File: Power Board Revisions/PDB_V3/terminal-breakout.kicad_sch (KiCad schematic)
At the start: 13 parts, among them J1 1017507, SW1 SW_SPST, SW13 SW_SPST, SW17 SW_SPST, SW21 SW_SPST, SW5 SW_SPST, SW9 SW_SPST

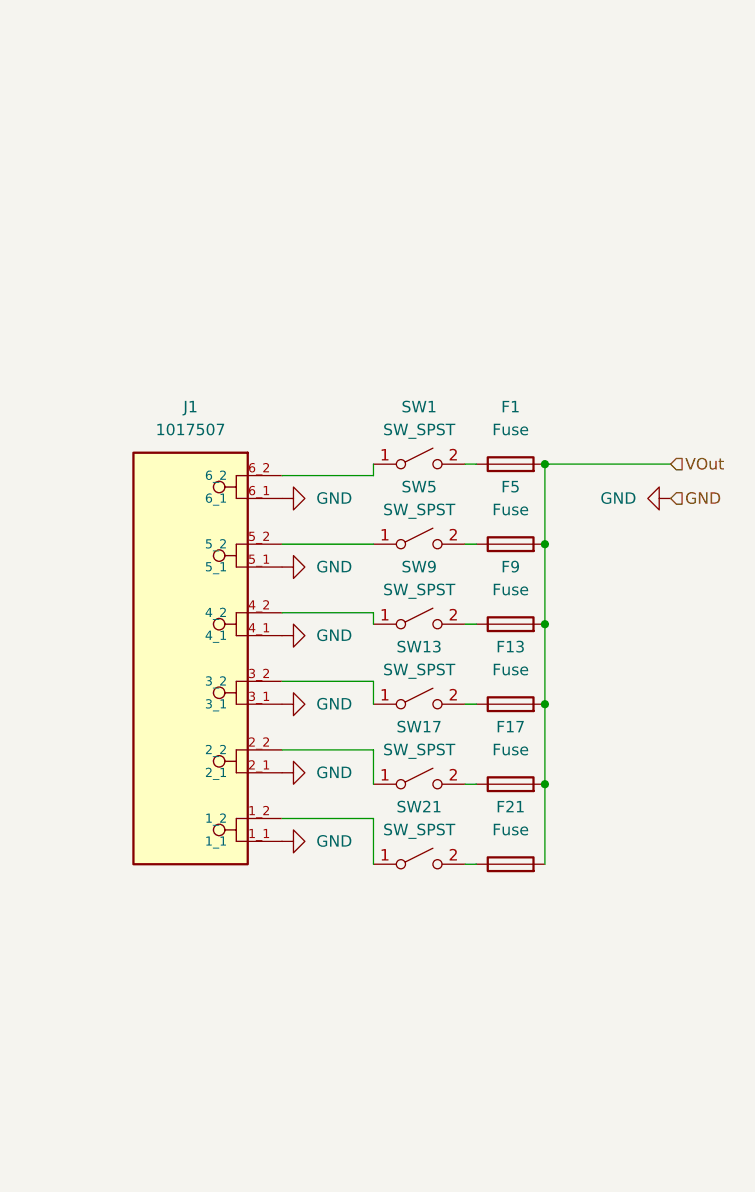
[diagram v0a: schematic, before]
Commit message: Updated PDB V3
I dislike KiCad on windows
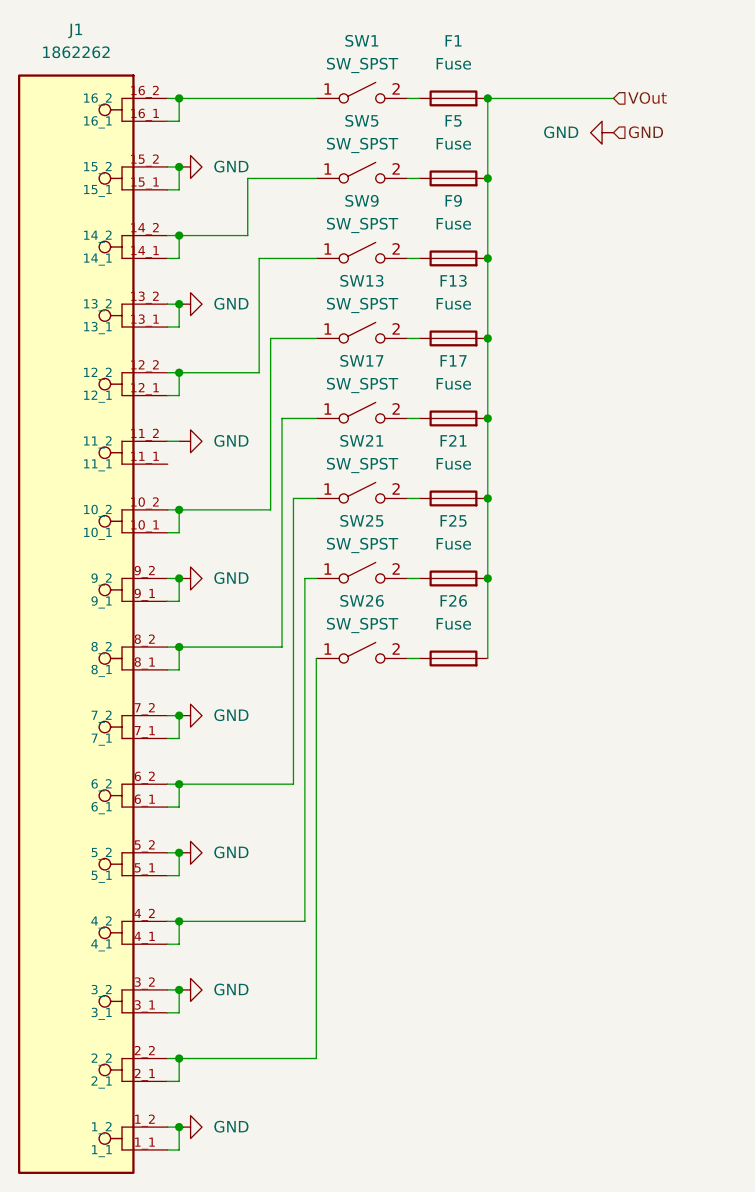
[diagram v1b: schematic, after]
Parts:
- removed J1: 1017507, Footprints:Phoenix 1017507, symbol Symbols:1017507
- added F25, F26: Fuse, Footprints:FUSE_3557-2, symbol Device:Fuse
- added J1: 1862262, Footprints:PHOENIX 1862262, symbol Symbols:1862262
- added SW25, SW26: SW_SPST, Footprints:ESwitch 1101A4CQEA, symbol Switch:SW_SPST
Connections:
- net GND: now also J1.11_2, J1.13_1, J1.13_2, J1.15_1, J1.15_2, J1.1_1, J1.1_2, J1.3_1, J1.3_2, J1.5_1, J1.5_2, J1.7_1, J1.7_2, J1.9_1, J1.9_2
- net VOut: now also F25.2, F26.2
- net at SW9.1 (A): now also J1.12_1, J1.12_2
- net at SW17.1 (A): now also J1.8_1, J1.8_2
- net at SW21.1 (A): now also J1.6_1, J1.6_2
- net at SW5.1 (A): now also J1.14_1, J1.14_2
- net at SW13.1 (A): now also J1.10_1, J1.10_2
- net at SW1.1 (A): now also J1.16_1, J1.16_2
- new net: F25.1, SW25.2 (B)
- new net: J1.2_1, J1.2_2, SW26.1 (A)
- new net: F26.1, SW26.2 (B)
- new net: J1.4_1, J1.4_2, SW25.1 (A)
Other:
- moved on the sheet: F1, F13, F17, F21, F5, F9, SW1, SW13, SW17, SW21, SW5, SW9

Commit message: Finalized PDB V3 for first design review
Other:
- company: (none) -> University of Guelph Robotics Team
- title: (none) -> 16P Terminal Breakout
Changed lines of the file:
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@@
 	(generator_version "10.0")
 	(paper "A4")
+	(title_block
+		(title "16P Terminal Breakout")
+		(date "2026-07-15")
+		(rev "1")
+		(company "University of Guelph Robotics Team")
+	)
 	(junction
 		(at 137.16 43.18)
